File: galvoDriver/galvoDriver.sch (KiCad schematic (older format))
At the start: 11 parts

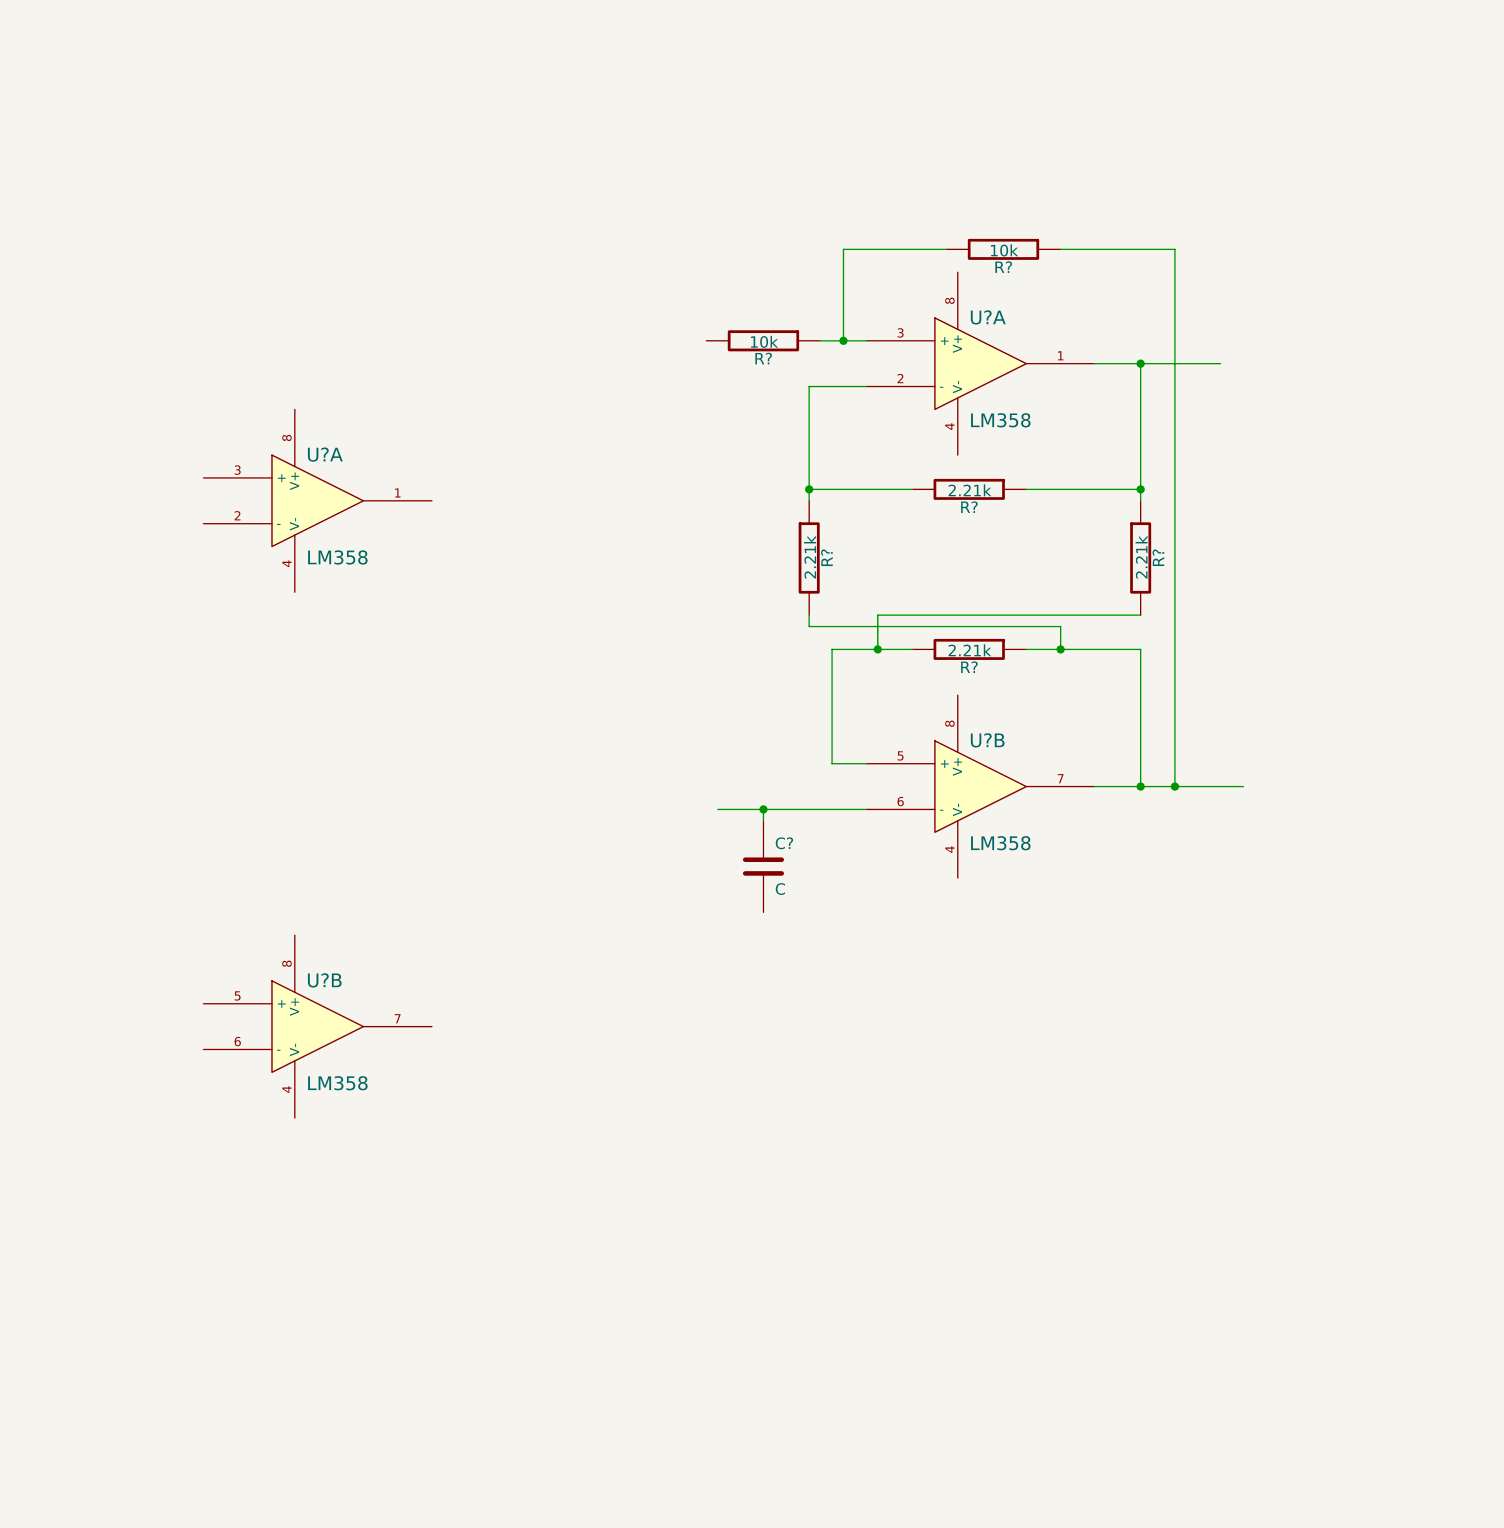
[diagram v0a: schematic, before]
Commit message: Op-amp circuit done (I think)
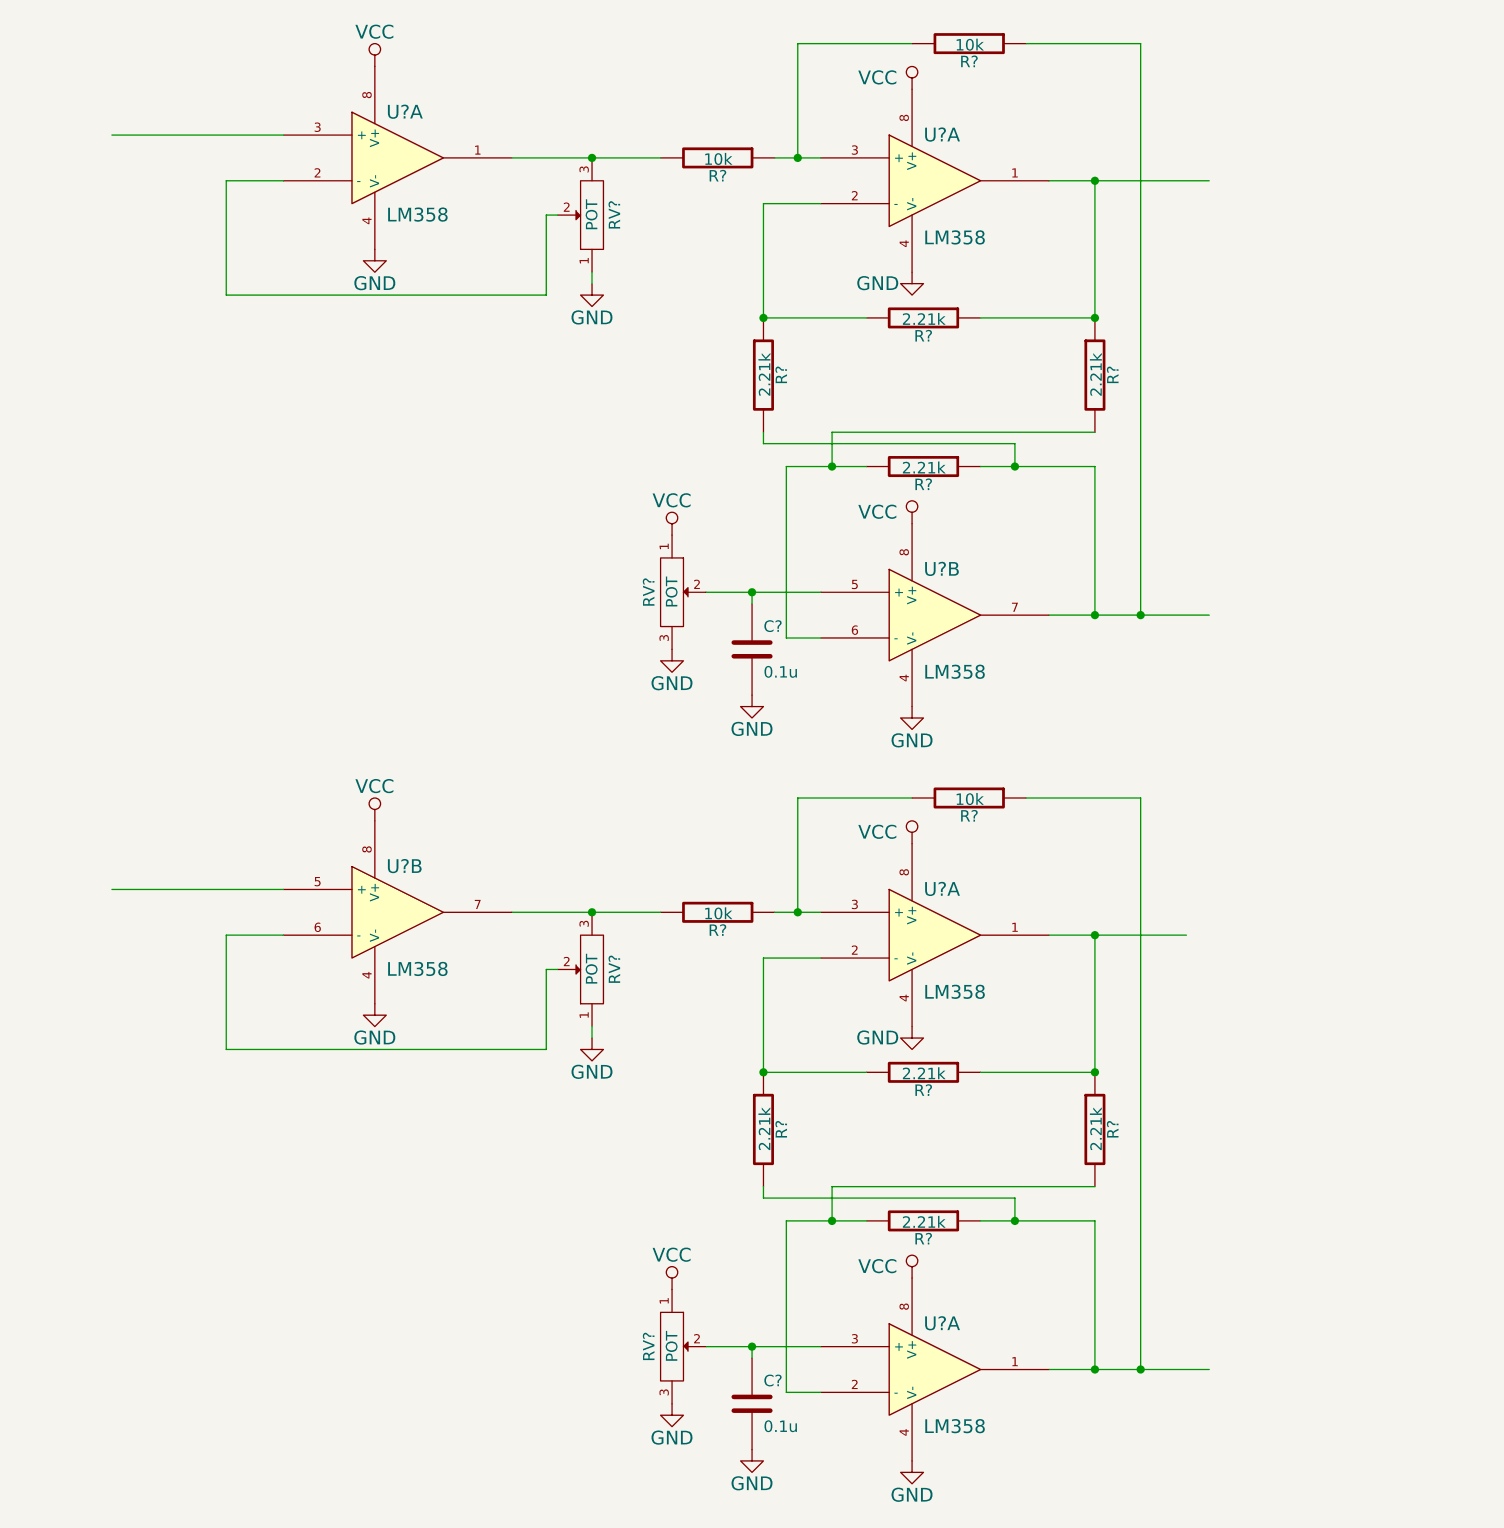
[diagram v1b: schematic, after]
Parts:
- added C?: 0.1u, symbol C
- added R? (x2): 10k, symbol R
- added R? (x4): 2.21k, symbol R
- added RV? (x4): POT, symbol POT
- added U? (x2): LM358, symbol LM358
- C?: value C -> 0.1u
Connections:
- net labels added: GND, VCC
- wire segments 24 -> 80
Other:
- moved on the sheet: C?, R?, U?A, U?B

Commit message: Added terminals for galvoDriver
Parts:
- added JP? (x5): M02, symbol M02
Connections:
- net labels added: xin, xout+, xout-, yin, yout+, yout-
- wire segments 80 -> 96

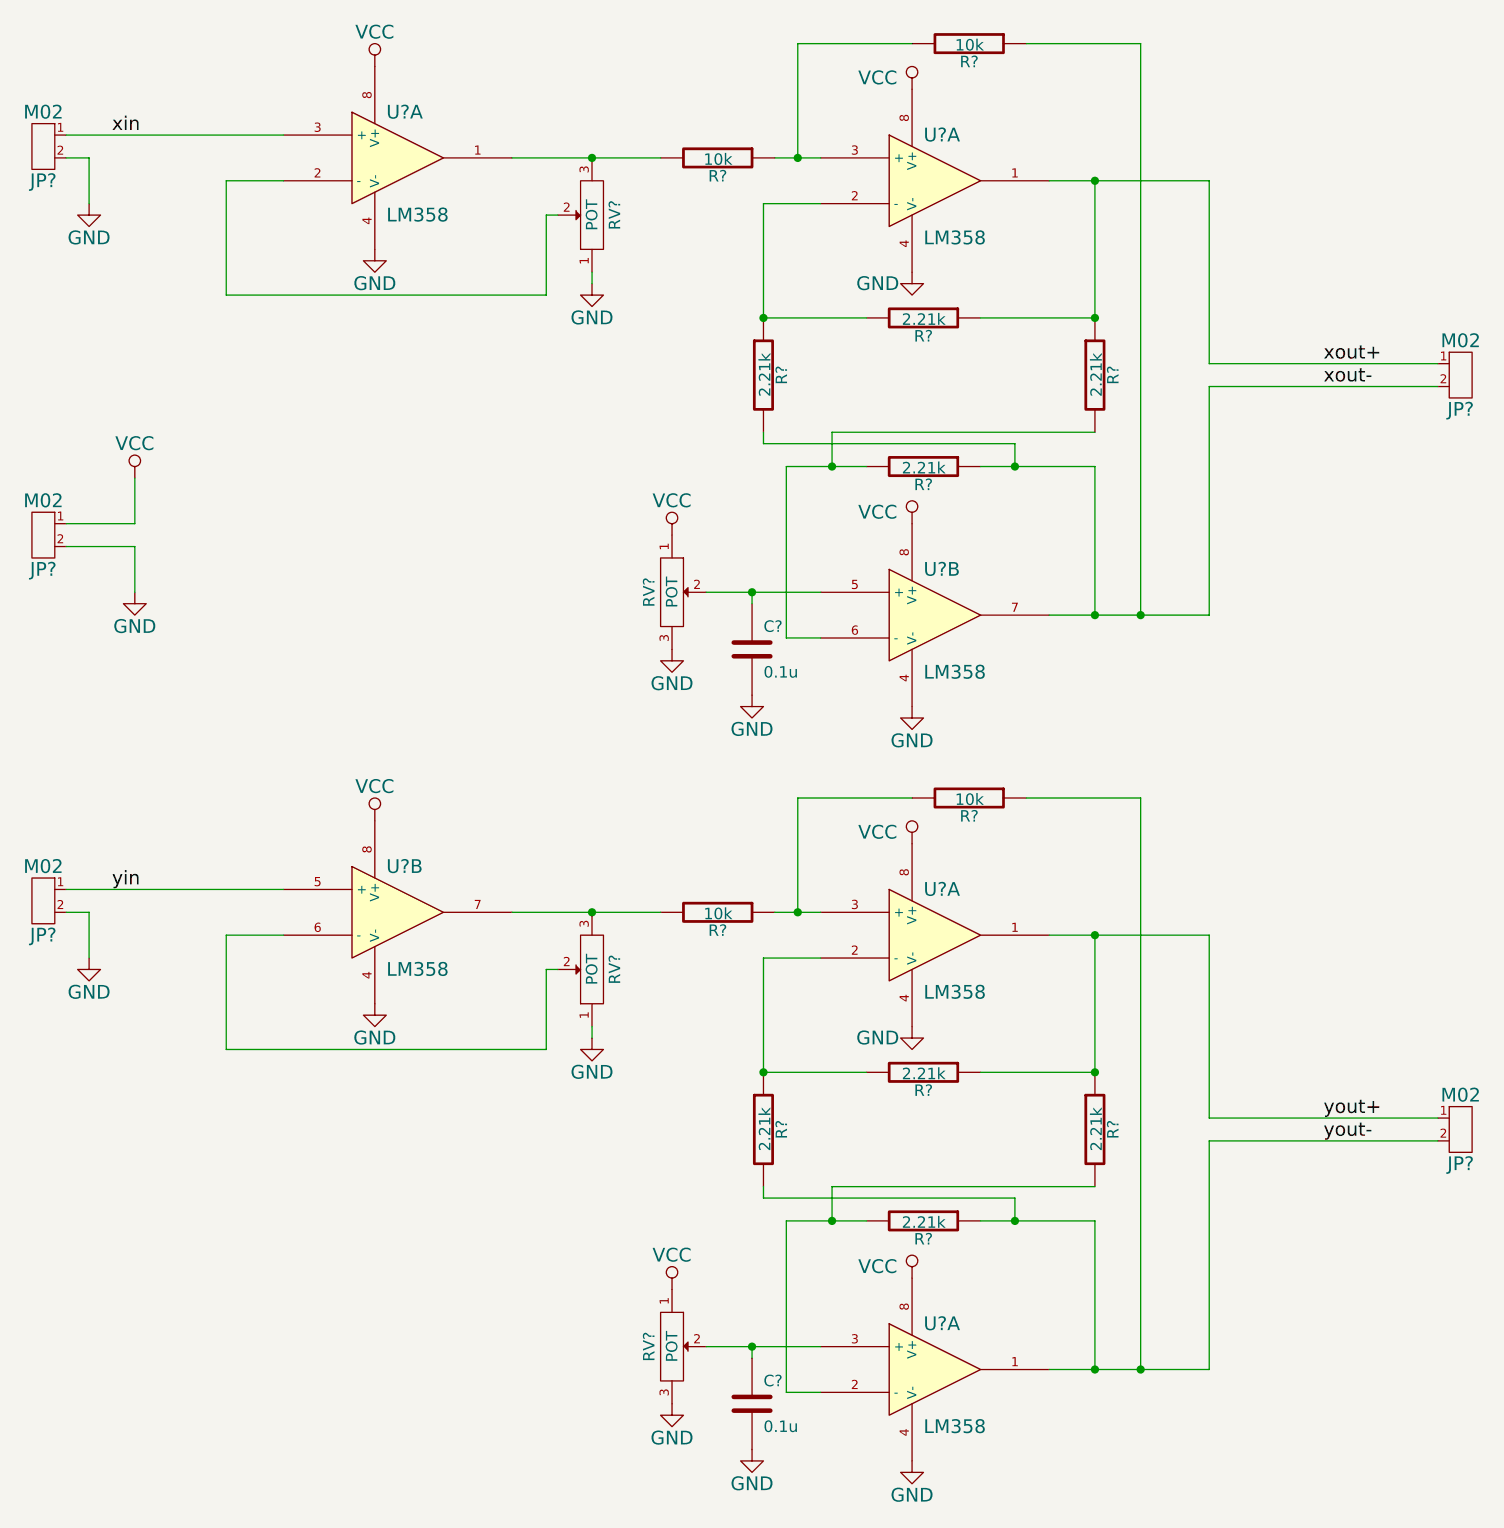
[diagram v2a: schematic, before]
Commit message: Annotating schematic
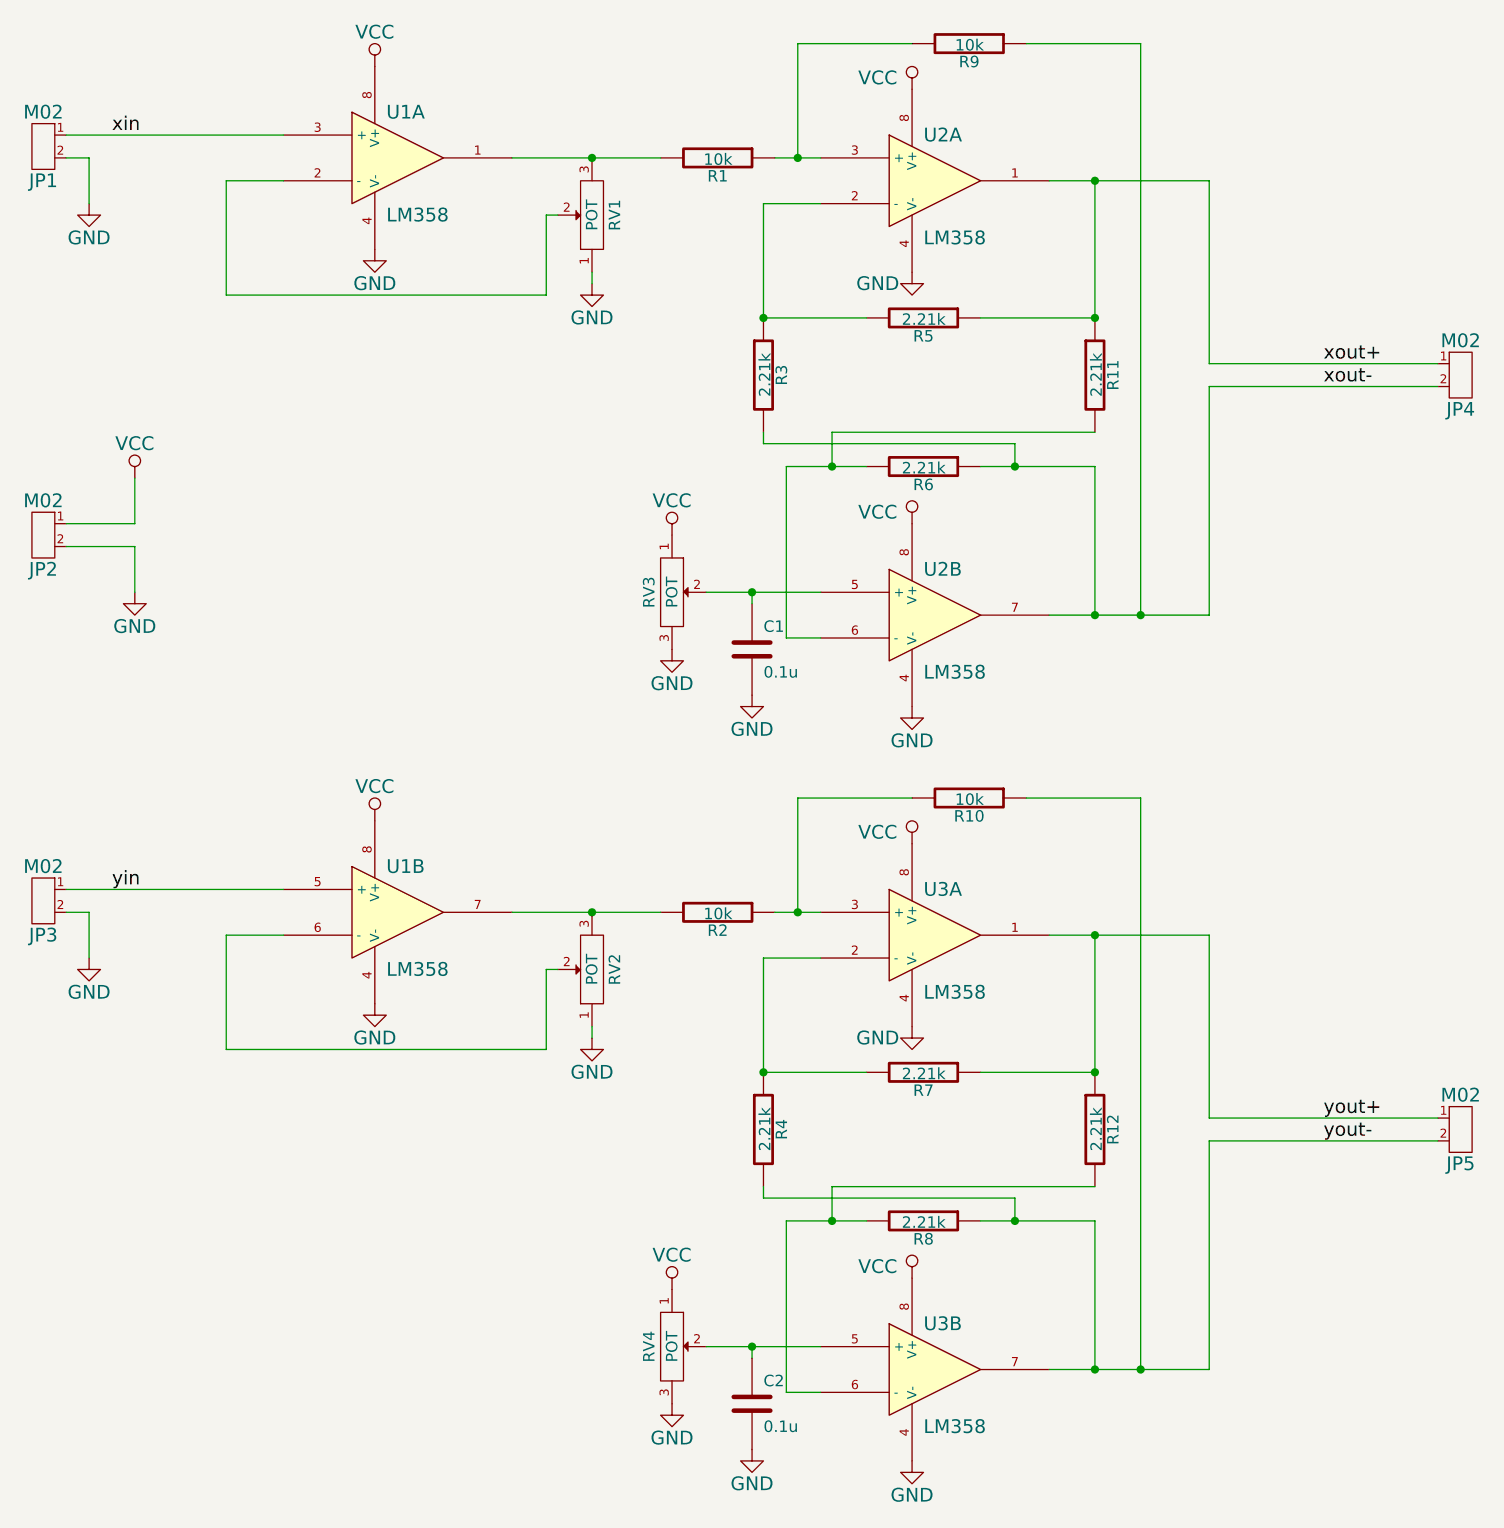
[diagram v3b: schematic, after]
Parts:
- gave numbers to parts that had none: 26
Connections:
- net yout-: now also U3.7; no longer U3.1
- net at R12.2, R8.2: now also U3.6 (-); no longer U3.2 (-)
- net at C2.1, RV4.2: now also U3.5 (+); no longer U3.3 (+)
